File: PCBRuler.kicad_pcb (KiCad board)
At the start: 2 copper layers, 170 x 25 mm, 17 parts, among them SW1 SW_PUSH, SW2 SW_PUSH, SW3 SW_PUSH, SW4 SW_PUSH

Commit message: changed backside centimeters for inches with lines at 100mils, 50 and 10
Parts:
- removed the Ref** at (178.0, 15.5)
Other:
- board text added: "INCHES"

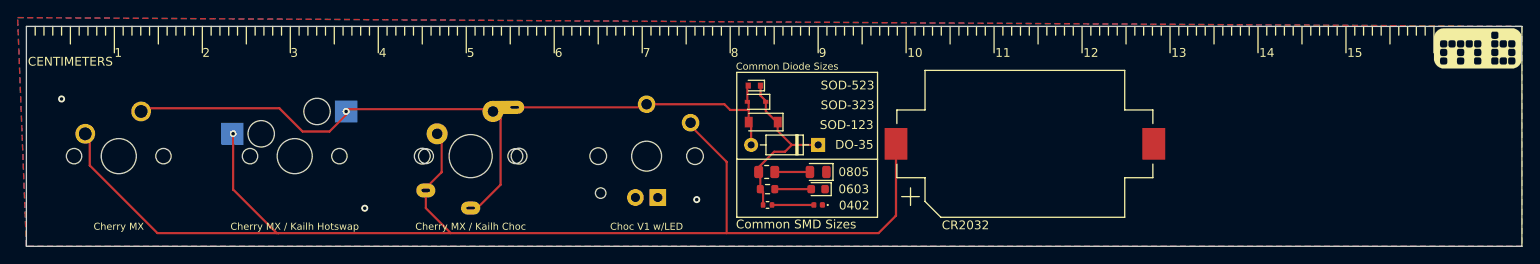
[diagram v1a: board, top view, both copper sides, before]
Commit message: moved some parts about, changed battery holder, added markings to top and bottom on both sides (alternated)
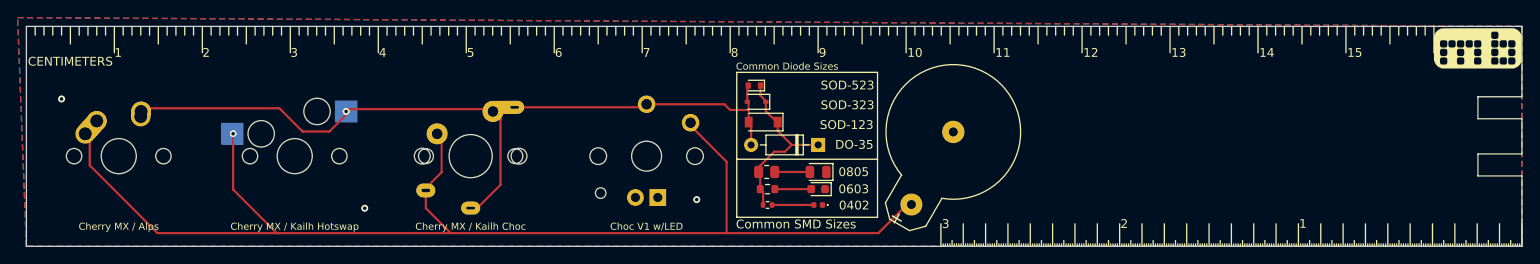
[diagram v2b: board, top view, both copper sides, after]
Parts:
- BT1: footprint Battery:BatteryHolder_Keystone_1060_1x2032 -> Battery:BatteryHolder_Keystone_500
- SW1: footprint MX_Only:MXOnly-1U-NoLED -> MX_Alps_Hybrid:MX-1U-NoLED
- moved BT1 14.6 mm to (113.6, 33.2), turned to 60 degrees
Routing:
- net Net-(BT1-Pad1): track 148.9 -> 142.5 mm
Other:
- outline, holes or cut-outs redrawn
- board text added: "Cherry MX / Alps"
- board text added: "This slot exists so you can bend component legs"
- board text removed: "CR2032"
- board text removed: "Cherry MX"
